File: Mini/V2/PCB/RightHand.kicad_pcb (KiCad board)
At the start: 2 copper layers, 155.9 x 99.3 mm, 30 parts

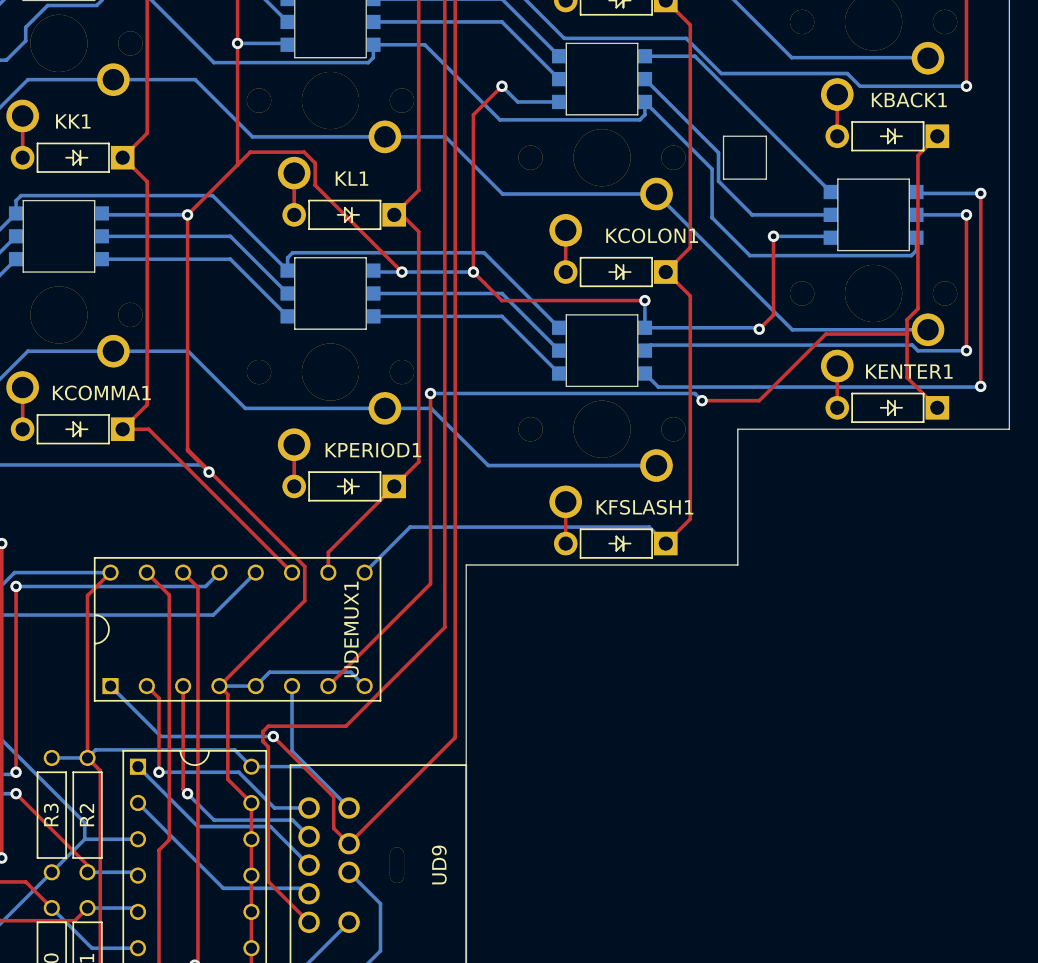
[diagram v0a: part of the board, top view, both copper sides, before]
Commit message: Updating LH PCB register to read 01 for register[4..5] and RH to read 10.  V1 will read as 00 for controller logic backward compatibility.
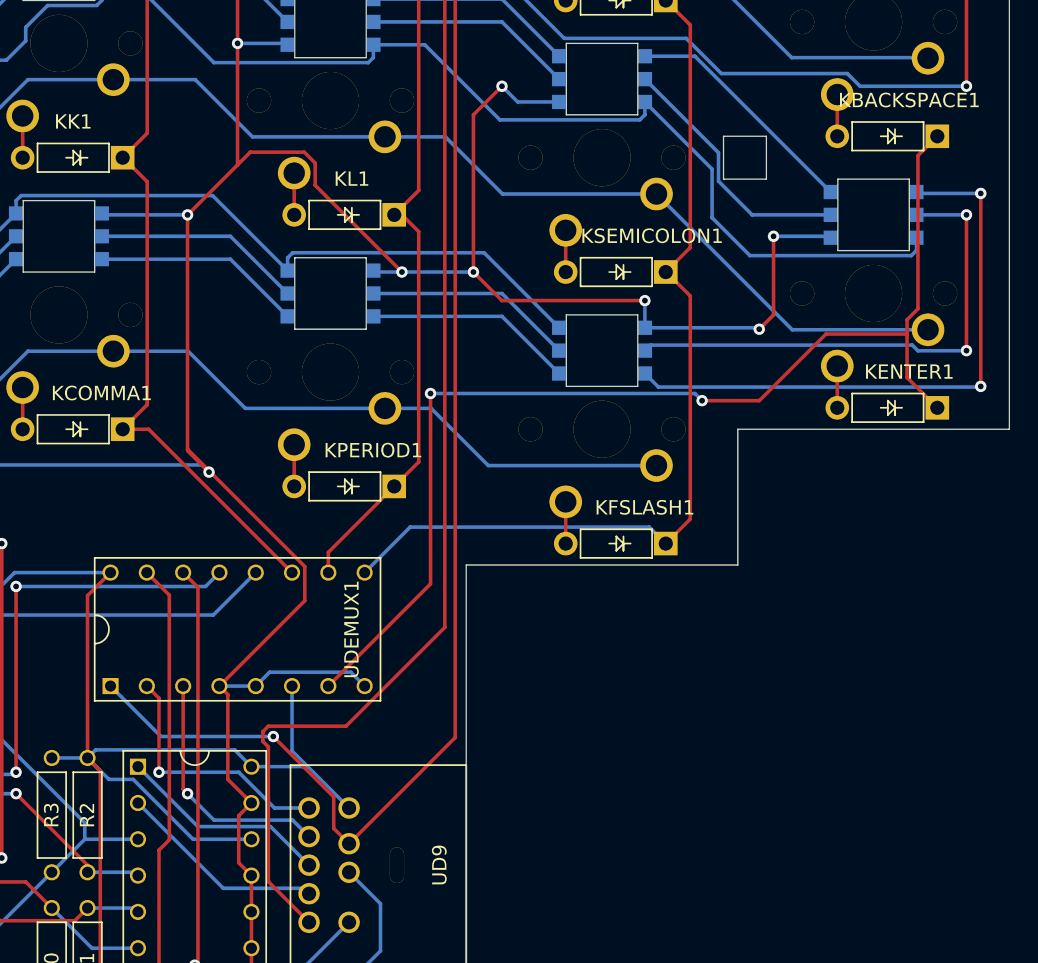
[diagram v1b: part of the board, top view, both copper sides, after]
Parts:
- renumbered KBACK1 to KBACKSPACE1, KCOLON1 to KSEMICOLON1
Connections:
- UREG1 pad 14: GND -> VCC
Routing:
- net VCC: track 597.6 -> 611.4 mm
- net GND: track 631.1 -> 631.8 mm

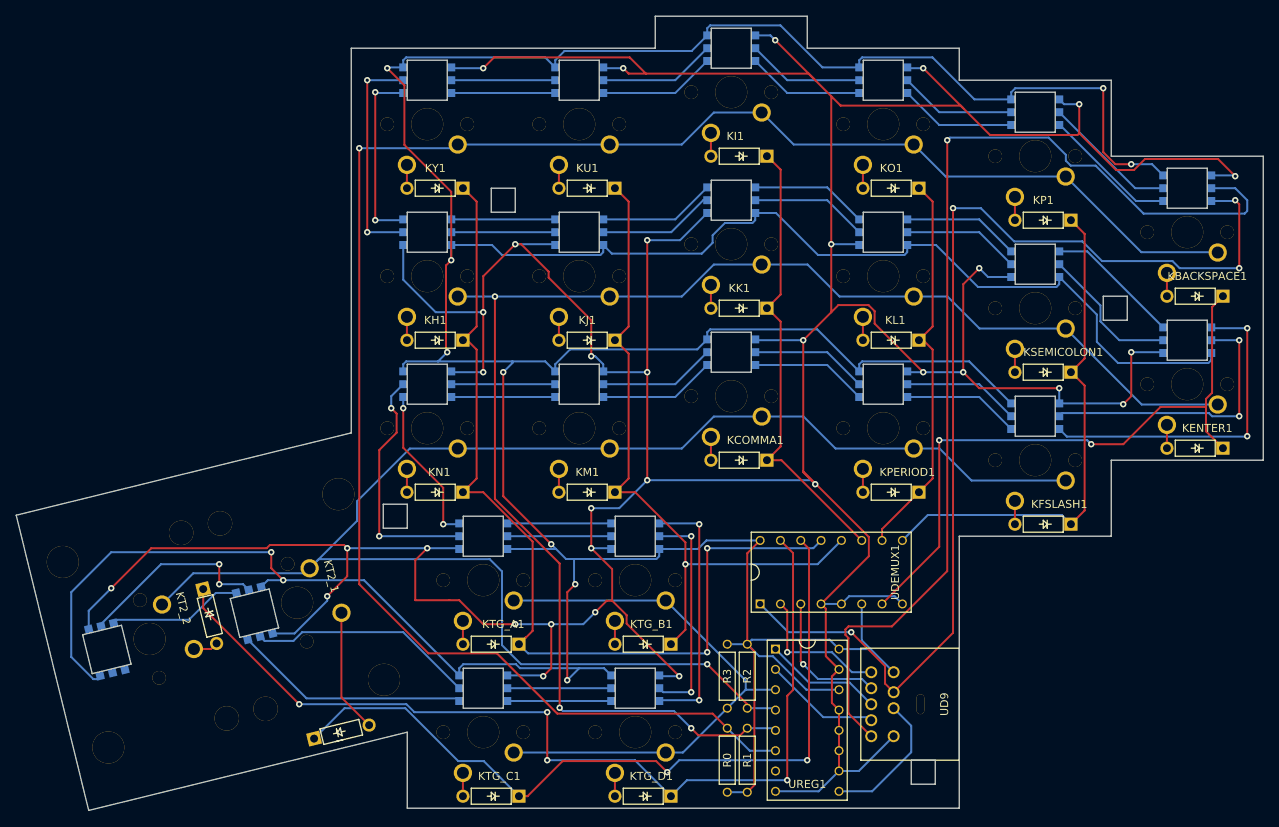
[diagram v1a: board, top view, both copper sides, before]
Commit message: Making all PCB adjustments to the right hand and regenerating gerber files.
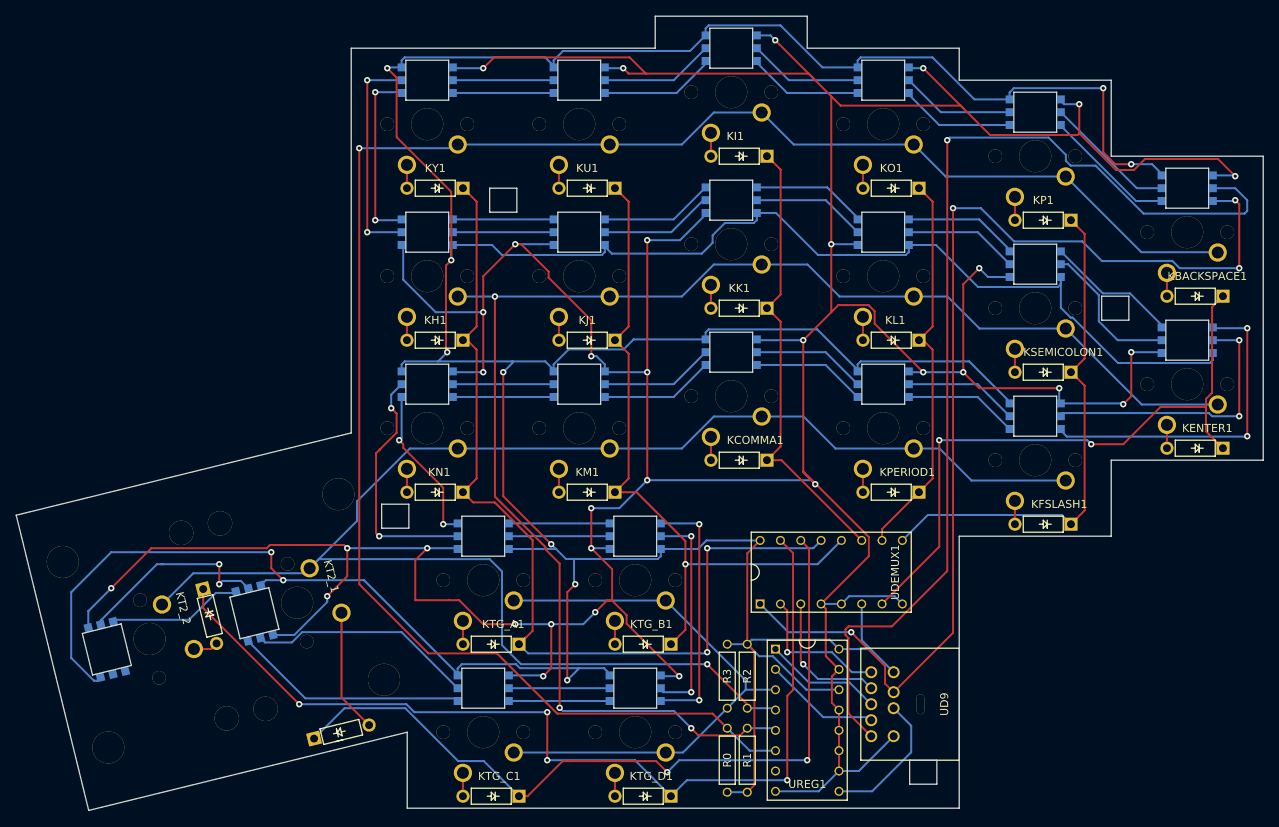
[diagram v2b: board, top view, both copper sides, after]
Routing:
- net VCC: track 611.4 -> 614.2 mm
- net Net-(KT2_1-Pad6): track 24.6 -> 25.2 mm
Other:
- outline, holes or cut-outs redrawn
